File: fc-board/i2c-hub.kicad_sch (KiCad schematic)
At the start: 26 parts, among them J4 M80-5102622, J5 SMA-J-P-X-ST-TH1, U3 ADS1015BQDGSRQ1, U4 PCT2075TP_147, U5 DS3231M+TRL

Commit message: Removed zips; updated gitignore
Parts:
- removed R15: 1M, Resistor_SMD:R_1206_3216Metric, symbol Device:R_Small
- removed R27: 1k, Resistor_SMD:R_1206_3216Metric, symbol Device:R_Small
- removed U3: ADS1015BQDGSRQ1, fc-board:ADS1015BQDGSRQ1, symbol fc-board:ADS1015BQDGSRQ1
- added C27: 1u, Capacitor_SMD:C_1206_3216Metric, symbol Device:C_Small
- added C28, C30, C32, C34: 1u, symbol Device:C_Small
- added C29: 10u, symbol Device:C_Small
- added C31, C33, C35: 0.1u, symbol Device:C_Small
- added CR10, CR5, CR6, CR7, CR8, CR9: BAS7002VH6327XTSA1, fc-board:BAS7002VH6327XTSA1, symbol fc-board:BAS7002VH6327XTSA1
- added R20, R22, R24, R26, R27, R28, R30, R31, R32, R34, R35: 1M, Resistor_SMD:R_1206_3216Metric, symbol Device:R_Small
- added R21: 180k, Resistor_SMD:R_1206_3216Metric, symbol Device:R_Small
- added R23: 531k, Resistor_SMD:R_1206_3216Metric, symbol Device:R_Small
- added R25: 347k, Resistor_SMD:R_1206_3216Metric, symbol Device:R_Small
- added R27: 2k, Resistor_SMD:R_1206_3216Metric, symbol Device:R_Small
- added R29: 500k, Resistor_SMD:R_1206_3216Metric, symbol Device:R_Small
- added R33: 263k, Resistor_SMD:R_1206_3216Metric, symbol Device:R_Small
- added U11: ADS122C04IPWR, fc-board:ADS122C04IPWR, symbol fc-board:ADS122C04IPWR
- added U12: REF3425TIDBVR, fc-board:REF3425TIDBVR, symbol fc-board:REF3425TIDBVR
- added U3: MAX11617EEE+, fc-board:MAX11617EEE+, symbol fc-board:MAX11617EEE+
- added U4: TLV9004QPWRQ1, fc-board:TLV9004QPWRQ1, symbol fc-board:TLV9004QPWRQ1
- R14: value 750k -> 5k
- R16, R17: value ??? -> 9.8k
- R19: value 220k -> 200k
- renumbered CR5 to CR2, CR2 to CR?, U4 to U5, U5 to U6
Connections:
- net 3.3V_IN: now also R14.1, C32.2, C33.2, C34.2, C35.2, CR10.1, CR5.1, CR6.1, CR7.1, CR8.1, CR9.1, U11.12 (AVDD), U11.13 (DVDD), U3.16 (VDD)
- net BIAS_IN: now also R17.1, U11.11 (AIN0)
- net BP: now also CR8.2, R30.1, R31.1, U3.11 (AIN6); no longer CR3.2, R14.1
- net GND: now also C27.1, C28.1, C29.1, C30.1, C31.1, C32.1, C33.1, C34.1, C35.1, R23.2, R27.2, R31.2, R33.2, R35.2, U11.1 (A0), U11.2 (A1), U11.4 (DGND), U11.5 (AVSS), U11.8 (REFN), U12.2 (GND), U3.15 (GND), U4.10 (IN3+), U4.11 (V-), U4.12 (IN4+), U4.3 (IN1+), U4.5 (IN2+); no longer R17.2
- net SCL: now also U11.16 (SCL), U3.13 (SCL)
- net SDA: now also U11.15 (SDA), U3.14 (SDA)
- net 15V_BBA renamed +15V_BBA
- net 5V_BP: no longer names the net of R14.2
- net 5V_BP: now also U11.14 (DRDY)
- net ??V_SIPM: no longer names the net of R16.2
- net ??V_SIPM: now also R17.2, C29.2, C30.2, C31.2, U11.9 (REFP), U12.6 (OUT)
- net BUBBA renamed +BUBBA
- net +BUBBA: now also U3.5 (AIN0)
- removed net SIPM: CR4.2, R16.1, R17.1
- new net: R27.1, U3.1 (AIN11/REF)
- new net: C27.2, R27.2
- new net: R20.1, R21.2, U4.2 (IN1-)
- new net: C28.2, U12.4 (IN)
- new net: R28.1, R29.2, U4.9 (IN3-)
- new net: R24.1, R25.2, U4.6 (IN2-)
- new net: U4.13 (IN4-), U4.14 (OUT4)
- new net +12V_HEAT: R32.2
- new net +5V_BP: R30.2
- new net +5V_CM4: R34.2
- new net +5V_SIPM: R26.2
- new net +7V2_CMT: R22.2
- new net +CREMAT: CR4.2, R22.1, R23.1, U3.7 (AIN2)
- new net +SIPM: CR6.2, R26.1, R27.1, U3.9 (AIN4)
- new net -15V_BBA: R20.2
- new net -5V_SIPM: R28.2
- new net -7V2_CMT: R24.2
- new net -BUBBA: CR3.2, R21.1, U3.6 (AIN1), U4.1 (OUT1)
- new net -CREMAT: CR5.2, R25.1, U3.8 (AIN3), U4.7 (OUT2)
- new net -SIPM: CR7.2, R29.1, U3.10 (AIN5), U4.8 (OUT3)
- new net ADS_RESET: U11.3 (RESET)
- new net BIAS_REF: R16.1, U11.10 (AIN1)
- new net CM4: CR10.2, R34.1, R35.1, U3.4 (AIN8)
- new net HEATER: CR9.2, R32.1, R33.1, U3.12 (AIN7)
- no-connect marks 1 -> 3
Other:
- note added: "+V BYPASS CAP(S)"
- note added: "Bias voltage sensing"
- note added: "DONT NEED THIS ANYMORE; REPLACE WITH ONE 4 PIN CONNECTION"
- note added: "Need to step down inputs to max 3.3V; All dividers are configured to output 2.5 V"
- note added: "Optional RC network shown in datasheet"
- note added: "Power voltage sensing"
- note added: "R16 and R17 form the second half of the voltage divider started on the bias board; with 150k and 9.8k, our bias ranges from 1.99 to 3 V (corresponding to 32.4 to 48 V) across the digipot range"
- note added: "REF datasheet recommends "low-ESR, low-inductance ceramic chip-type output capacitors (X5R, X7R, or similar)" for the bypass caps"
- note added: "REWORK USING NEW VOLTAGE RANGE 32.4 - 48.8 V"
- note added: "This is for sensing all of the switching supply voltages."
- note added: "Tying both to DGND sets addr to 0x40"
- note added: "Unused inputs can be left floating (AIN2, AIN3)"
- note removed: "ADC and inputs for thermocouples?"
- note removed: "Need to step down to max 3.3V 5 V -> 3.0 V with R15 = 1 MOhm requires R14 = 667 kOhm"
- note removed: "Schottky diode for overvoltage protection. Could use 3.3V zener diode instead."
- note removed: "Tying ADDR to GND sets address to 0x48"
- note removed: "Voltage sensing ADC"
- moved on the sheet: C3, C4, C5, CR2, CR?, J4, J5, JP4, R10, R11, R12, R13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

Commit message: Fc board (#9)
* FC board updates

* Finished routing; cleaned library

* Updated RJ45 jack

* Assigned part numbers to everything, replaced ethernet jack

* Finalized layout

* V1 sent for printing
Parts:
- removed C28, C30: 1u, symbol Device:C_Small
- removed C29: 10u, symbol Device:C_Small
- removed C31: 0.1u, symbol Device:C_Small
- removed CR?: BAS7002VH6327XTSA1, fc-board:BAS7002VH6327XTSA1, symbol fc-board:BAS7002VH6327XTSA1
- removed J4: M80-5102622, fc-board:M80-5102622, symbol fc-board:M80-5102622
- removed J5: SMA-J-P-X-ST-TH1, fc-board:SMA-J-P-X-ST-TH1, symbol fc-board:SMA-J-P-X-ST-TH1
- removed JP4: VBAT GND, Jumper:SolderJumper-2_P1.3mm_Open_Pad1.0x1.5mm, symbol Jumper:SolderJumper_2_Open
- removed R10, R11: R_Small, Resistor_SMD:R_1206_3216Metric, symbol Device:R_Small
- removed R12: 1M, Resistor_SMD:R_1206_3216Metric, symbol Device:R_Small
- removed R13: 100k, Resistor_SMD:R_1206_3216Metric, symbol Device:R_Small
- removed U12: REF3425TIDBVR, fc-board:REF3425TIDBVR, symbol fc-board:REF3425TIDBVR
- added BT1: CR-1220_FCN, fc-board:CR-1220-FCN, symbol fc-board:CR-1220_FCN
- added C10: 0.1u, Capacitor_SMD:C_1206_3216Metric, symbol Device:C_Small
- added CR4: BAS7002VH6327XTSA1, fc-board:BAS7002VH6327XTSA1, symbol fc-board:BAS7002VH6327XTSA1
- added JP7: VBAT GND, Jumper:SolderJumper-2_P1.3mm_Open_Pad1.0x1.5mm, symbol Jumper:SolderJumper_2_Open
- added R15: 10k, Resistor_SMD:R_1206_3216Metric, symbol Device:R_Small
- added R32: 4.99k, Resistor_SMD:R_1206_3216Metric, symbol Device:R_Small
- added TP11: OS, fc-board:TestPoint_THTPad_D2.0mm_Drill1.0mm_JLCrules, symbol Connector:TestPoint
- added TP13: RST, fc-board:TestPoint_THTPad_D2.0mm_Drill1.0mm_JLCrules, symbol Connector:TestPoint
- C11: renamed from C35; footprint (none) -> Capacitor_SMD:C_1206_3216Metric
- C12: renamed from C34; footprint (none) -> Capacitor_SMD:C_1206_3216Metric
- C13: renamed from C33; footprint (none) -> Capacitor_SMD:C_1206_3216Metric
- C14: renamed from C32; footprint (none) -> Capacitor_SMD:C_1206_3216Metric
- C6: renamed from C27; value 1u -> 0.1u
- R14: value 5k -> 10k
- R18: renamed from R21; value 180k -> 71.5k
- R19: renamed from R25; value 347k -> 162k
- R20: renamed from R29; value 500k -> 249k
- R22: renamed from R17; value 9.8k -> 10k
- R23: renamed from R16; value 9.8k -> 10k
- R26: renamed from R19; value 200k -> 71.5k
- R27: renamed from R31; value 1M -> 249k
- R30: renamed from R23; value 531k -> 162k
- R31: renamed from R33; value 263k -> 90.9k
- R35: renamed from R27; value 1M -> 249k
- R36: renamed from R35; value 1M -> 249k
- TP12: renamed from TP1; value TestPoint -> PPS
- TP14: renamed from TP2; value TestPoint -> 32kHz
- renumbered C3 to C7, C5 to C8, C4 to C9, CR3 to CR1, CR5 to CR2, CR7 to CR3, CR2 to CR5, CR8 to CR6, CR4 to CR7, CR9 to CR8, CR6 to CR9, R27 to R13, R20 to R16, R24 to R17, R28 to R21, R18 to R24, R30 to R25, R22 to R28, R32 to R29, R26 to R33, U3 to U6, U6 to U7, U4 to U8, U11 to U9
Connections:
- net +5V_IN: now also U8.4 (V+), C10.1
- net +BUBBA: now also U6.11 (AIN6); no longer U6.5 (AIN0)
- net -SIPM: now also U6.5 (AIN0); no longer U6.10 (AIN5)
- net 3.3V_IN: now also CR4.1, R15.1, R32.1
- net 32kHz: now also R14.2
- net BIAS_IN: now also R23.1, CR4.2; no longer R22.1
- net BIAS_REF: now also R22.1; no longer R23.1
- net BP: now also U6.10 (AIN5); no longer U6.11 (AIN6)
- net GND: now also R22.2, R23.2, BT1.-, C10.2, JP7.1 (A); no longer U9.8 (REFN)
- net OS: now also TP11.1
- net PPS: now also U7.3 (*INT/SQW), R15.2
- net SCL: no longer U9.16 (SCL)
- net SDA: no longer U9.15 (SDA)
- net at U7.14 (VBAT): now also BT1.+, JP7.2 (B)
- net ADS_DRDY: now reaches U9.14 (DRDY)
- net ADS_DRDY: now also R32.2; no longer R14.2
- net RST: now reaches U7.4 (*RST)
- net RST: now also TP13.1
- new net BIAS_SCL: U9.16 (SCL)
- new net BIAS_SDA: U9.15 (SDA)
- now unconnected: U9.9 (REFP)
- no-connect marks 3 -> 6
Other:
- note added: "Address tied to 1/0/0 (A0/A1/A2), setting it to 0x49"
- note added: "Current limiting resistors: datasheet says 1k - 1M typical"
- note added: "Need to step down inputs to max 3.3V; All dividers are configured to output 1 V (about half of the 2.048 V ADC V_ref)"
- note added: "OUT4 is a GND follower"
- note added: "Swap to the ADS1120 (16 bit)? Although I think that one is SPI only..."
- note added: "These two resistors form the second half of the voltage divider started on the bias board; with 150k and 7k, our bias ranges from 1.427 to 2.176 V (corresponding to 32.4 to 48.8 V) across the digipot range. This is then added on the 1.024 V reference voltage."
- note added: "Tying both A0 & A1 to DGND sets addr to 0x40"
- note added: "Unsure what to do with REFN and REFP when unused. The datasheet doesn't mention..."
- note added: "We could invert the OS output and use that to completely automate heater toggles in hardware"
- note added: "What do we do with RST? No external pullup needed; there's an internal one."
- note removed: "+V BYPASS CAP(S)"
- note removed: "Current limiting resistor; what value do we want?"
- note removed: "DONT NEED THIS ANYMORE; REPLACE WITH ONE 4 PIN CONNECTION"
- note removed: "Do we need any decoupling capacitors here?"
- note removed: "External I2C connections"
- note removed: "Need to step down inputs to max 3.3V; All dividers are configured to output 2.5 V"
- note removed: "Need to step down to max 3.3V 32 V -> 3.3 V with R12 = 1 MOhm requires R13 = 115 kOhm"
- note removed: "OS output can be used to control heater. Control registers can be used to set temperature thresholds as well as the pin polarity."
- note removed: "R16 and R17 form the second half of the voltage divider started on the bias board; with 150k and 9.8k, our bias ranges from 1.99 to 3 V (corresponding to 32.4 to 48 V) across the digipot range"
- note removed: "REF datasheet recommends "low-ESR, low-inductance ceramic chip-type output capacitors (X5R, X7R, or similar)" for the bypass caps"
- note removed: "REWORK USING NEW VOLTAGE RANGE 32.4 - 48.8 V"
- note removed: "Tying both to DGND sets addr to 0x40"
- moved on the sheet: C11, C12, C13, C14, C7, C9, CR1, CR2, CR3, R16, R17, R18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

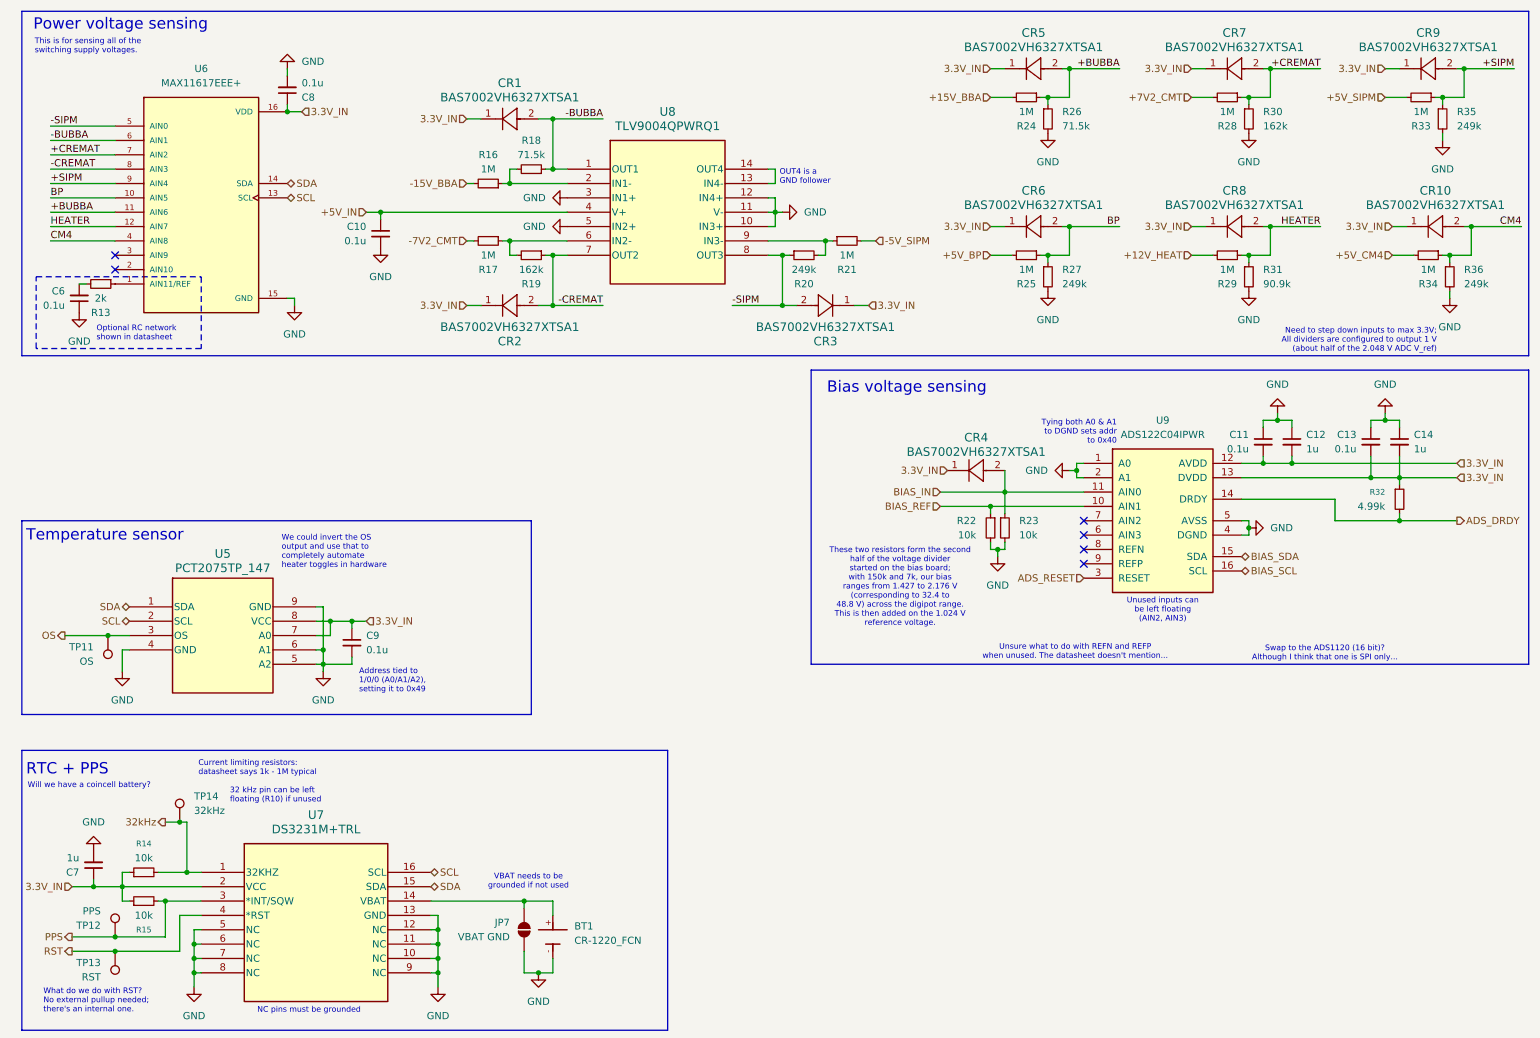
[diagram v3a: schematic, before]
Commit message: Fixed incorrect routes, modified gondola eth, cosmetics
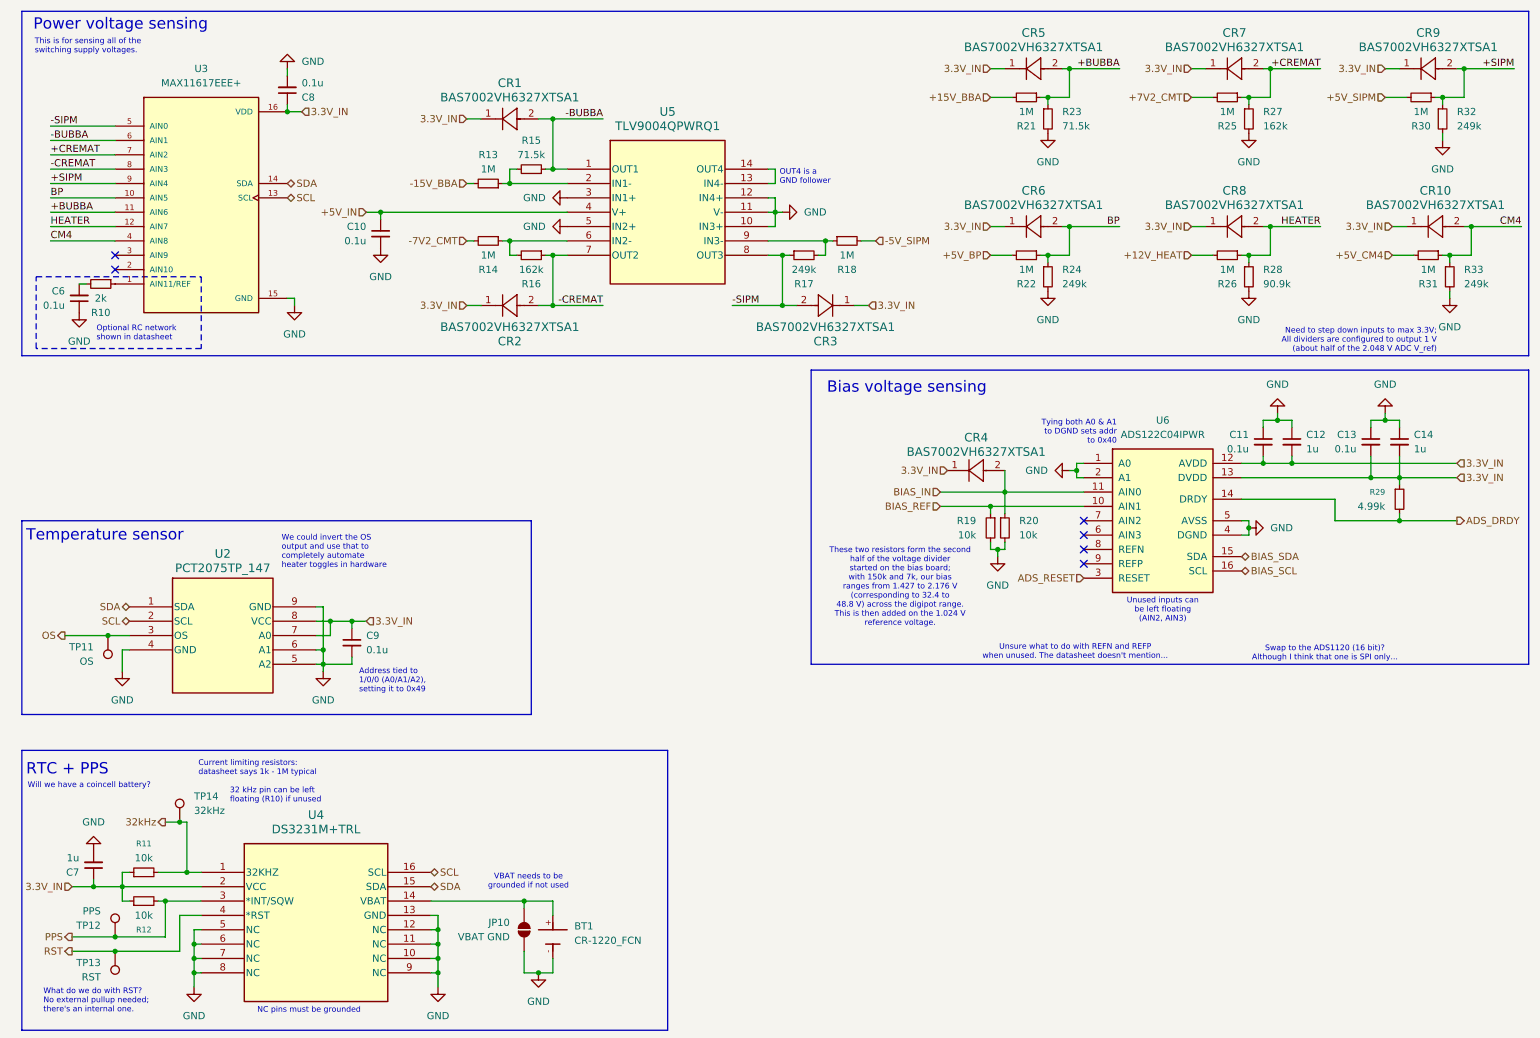
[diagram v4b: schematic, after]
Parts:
- renumbered JP7 to JP10, R13 to R10, R14 to R11, R15 to R12, R16 to R13, R17 to R14, R18 to R15, R19 to R16, R20 to R17, R21 to R18, R22 to R19, R23 to R20, R24 to R21, R25 to R22, R26 to R23, R27 to R24, R28 to R25, R29 to R26, R30 to R27, R31 to R28, R32 to R29, R33 to R30, R34 to R31, R35 to R32, R36 to R33, U5 to U2, U6 to U3, U7 to U4, U8 to U5, U9 to U6
